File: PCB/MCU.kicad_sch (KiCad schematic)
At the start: 33 parts

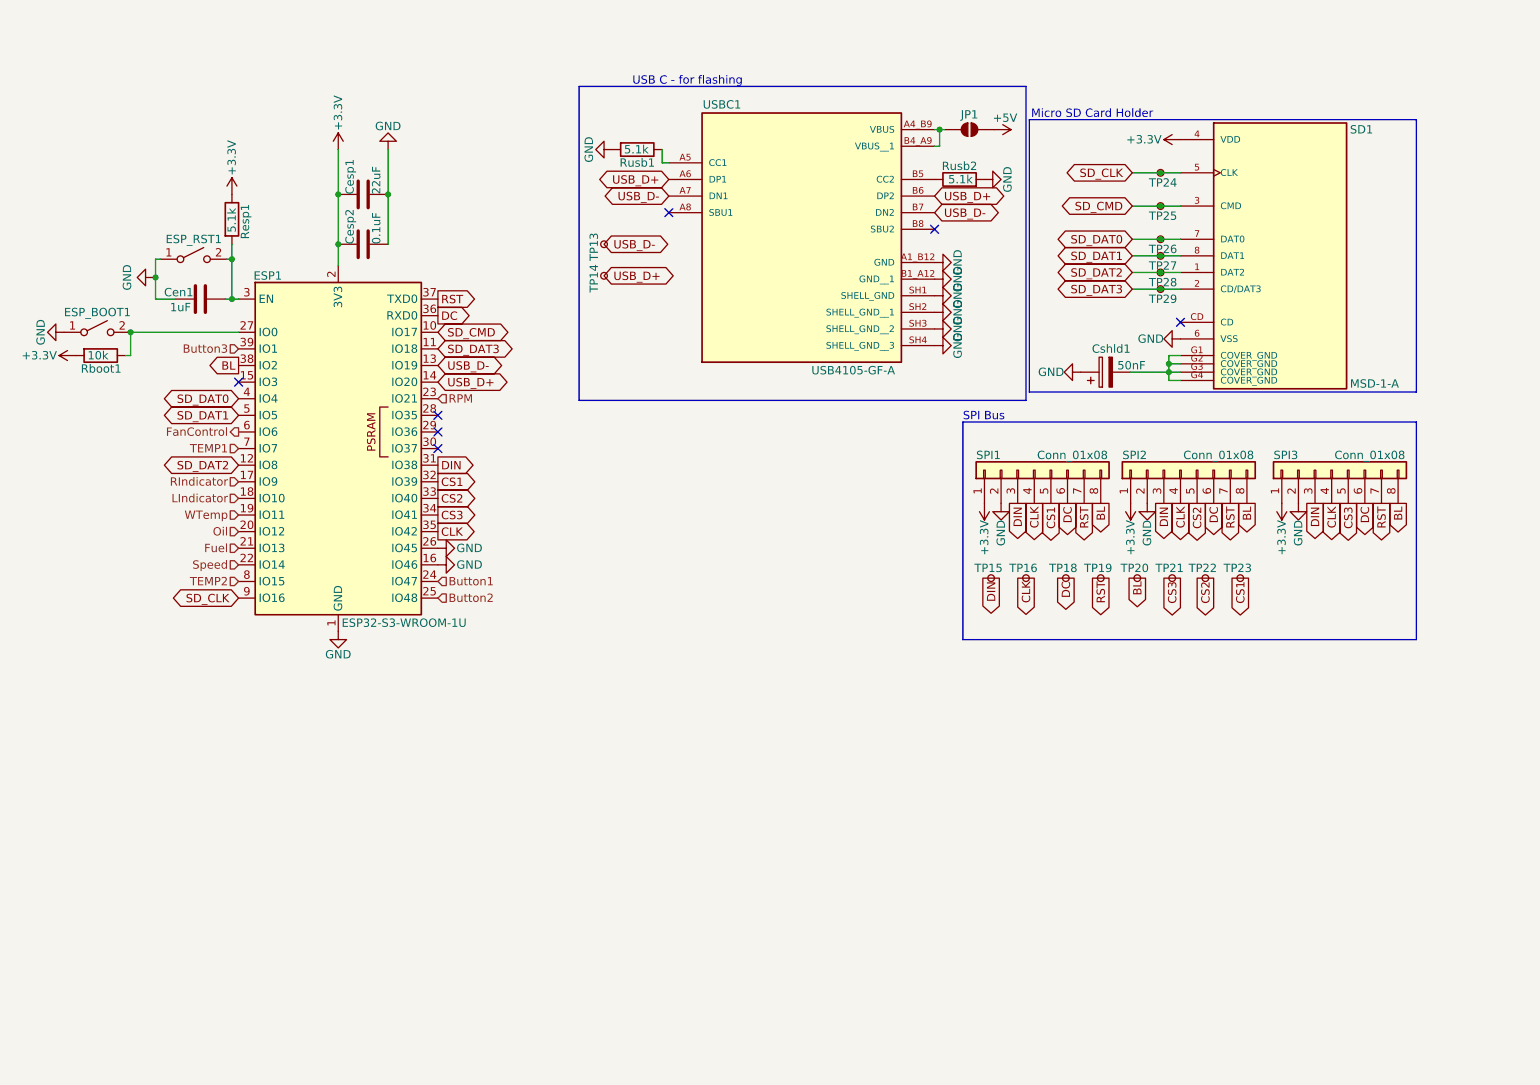
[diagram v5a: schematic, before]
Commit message: Redone Schematics for better readability (the circuitry didnt change
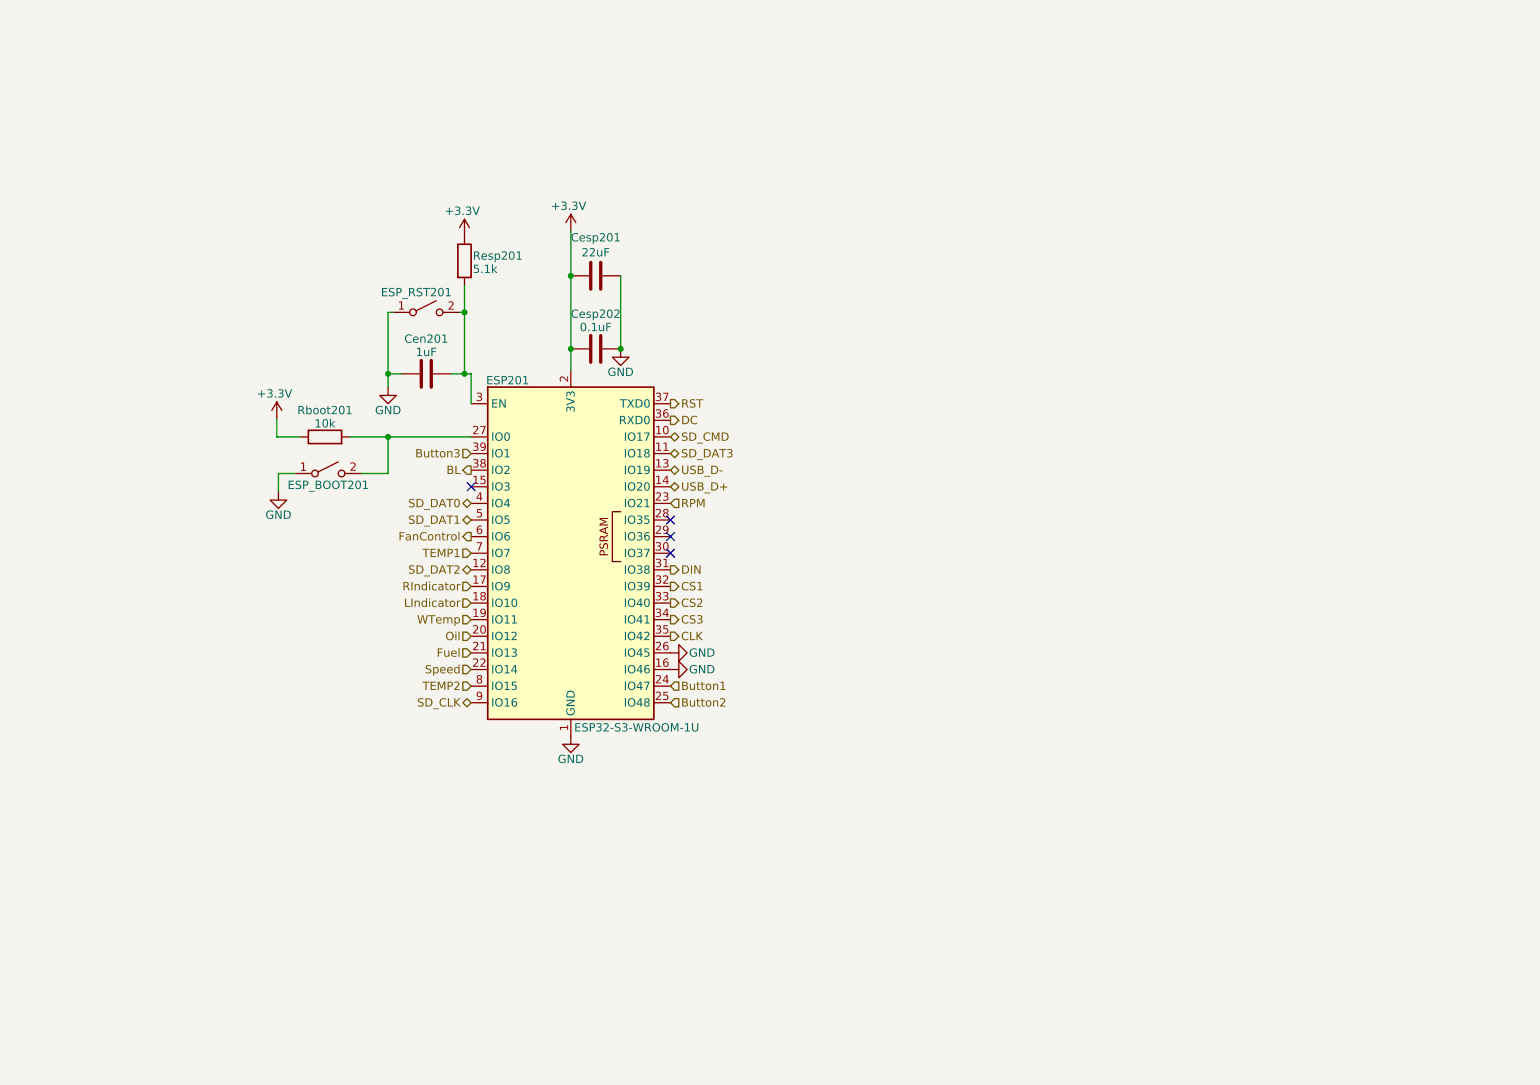
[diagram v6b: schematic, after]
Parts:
- removed Cshld1: 50nF, Capacitor_SMD:C_0805_2012Metric, symbol Device:C_Polarized
- removed JP1: SolderJumper_2_Open, Jumper:SolderJumper-2_P1.3mm_Open_TrianglePad1.0x1.5mm, symbol Jumper:SolderJumper_2_Open
- removed Rusb1, Rusb2: 5.1k, Resistor_SMD:R_0603_1608Metric, symbol Device:R
- removed SD1: MSD-1-A, MSD-1-A:CUI_MSD-1-A, symbol MSD-1-A:MSD-1-A
- removed SPI1, SPI2, SPI3: Conn_01x08, Connector_JST:JST_XH_S8B-XH-A_1x08_P2.50mm_Horizontal, symbol Connector_Generic:Conn_01x08
- removed TP13, TP14, TP15, TP16, TP18, TP19, TP20, TP21, TP22, TP23, TP24, TP25, TP26, TP27, TP28, TP29: TestPoint_Small, TestPoint:TestPoint_Pad_D1.0mm, symbol Connector:TestPoint_Small
- removed USBC1: USB4105-GF-A, USB-C 2.0:GCT_USB4105-GF-A, symbol USB-C:USB4105-GF-A
- renumbered Cen1 to Cen201, Cesp1 to Cesp201, Cesp2 to Cesp202, ESP1 to ESP201, ESP_BOOT1 to ESP_BOOT201, ESP_RST1 to ESP_RST201, Rboot1 to Rboot201, Resp1 to Resp201
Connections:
- net +3.3V: now also Rboot201.1; no longer Rboot201.2
- net at ESP201.27 (IO0), ESP_BOOT201.2 (B): now also Rboot201.2; no longer Rboot201.1
- no-connect marks 7 -> 4
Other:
- note removed: "Micro SD Card Holder"
- note removed: "SPI Bus"
- note removed: "USB C - for flashing"
- moved on the sheet: Cen201, Cesp201, Cesp202, ESP201, ESP_BOOT201, ESP_RST201, Rboot201, Resp201

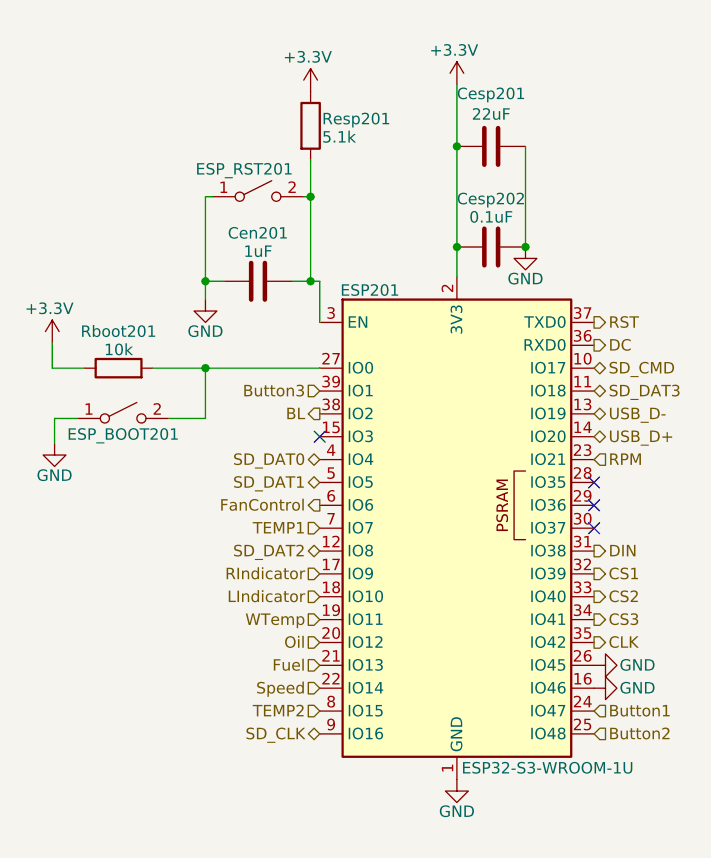
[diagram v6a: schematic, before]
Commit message: Applied recommendations from my coworker; Fixed badly placed filter caps; Added flyback diode to fan circuit; Applied larger grid and some spacing to the schematics; And some other small adjustments
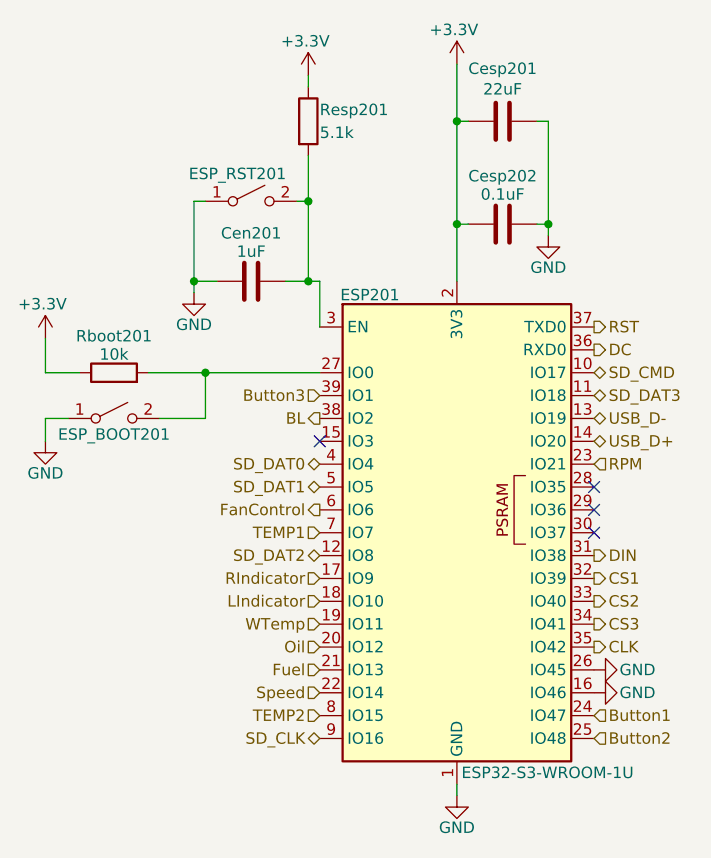
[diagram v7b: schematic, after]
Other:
- title: (none) -> MCU
- moved on the sheet: Cen201, Cesp201, Cesp202, ESP201, ESP_BOOT201, ESP_RST201, Rboot201, Resp201

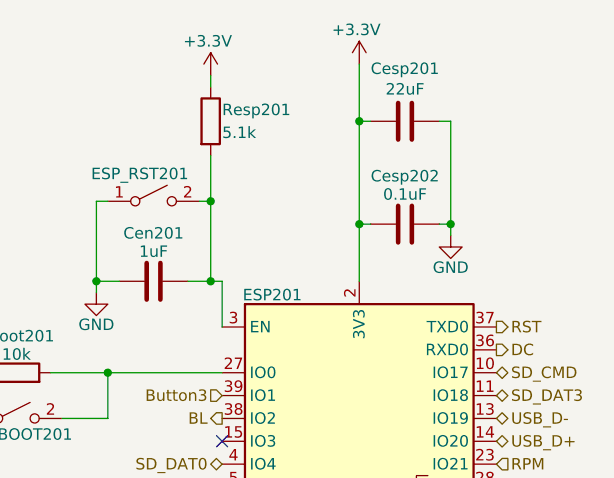
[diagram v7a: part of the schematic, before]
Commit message: Changed some resistor and capacitor values;Added additional input electrolytic cap;Selected LCSC parts;Added diode footprint;Removed 3.3V power supply and decreased the output of the 5V supply to 3.3V;Added flyback diode on the fan circuit;Added LDO between the USB-C VBUS and the 5V rail
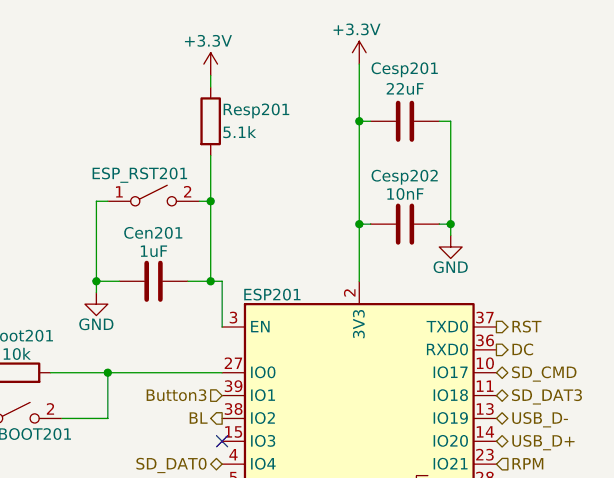
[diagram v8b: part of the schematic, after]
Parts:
- Cesp202: value 0.1uF -> 10nF
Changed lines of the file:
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@@
 			)
 		)
-		(property "Value" "0.1uF"
+		(property "Value" "10nF"
 			(at 154.94 61.468 90)
 			(effects
